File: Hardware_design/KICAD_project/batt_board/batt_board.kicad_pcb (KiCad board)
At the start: 2 copper layers, 50.8 x 50.8 mm, 41 parts, among them J11 battery_plug_in, J2 Conn_01x02, J3 Conn_01x02, J4 Conn_01x02, J5 Conn_01x02, U1 TPS5430DDA, U2 AMS1117-3.3

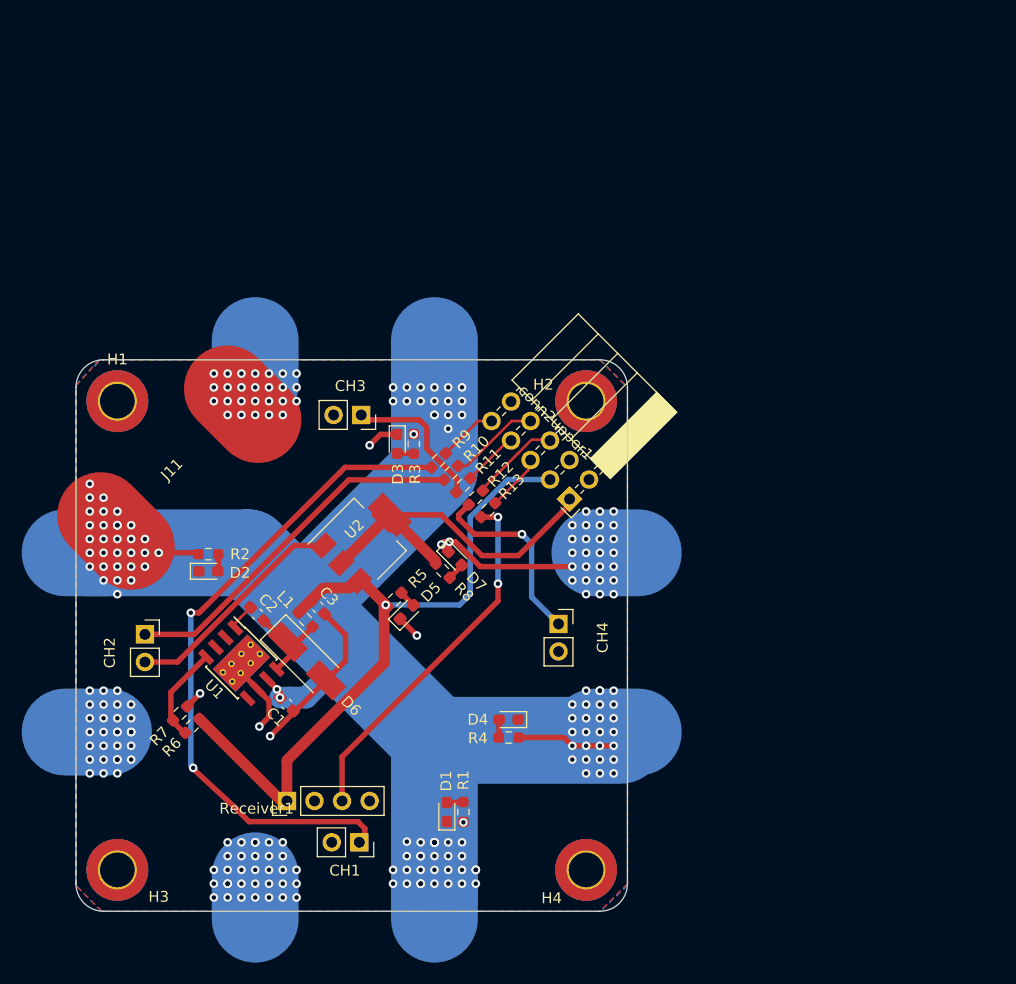
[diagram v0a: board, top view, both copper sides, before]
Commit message: battBoard 打板 control board 设备外设放置
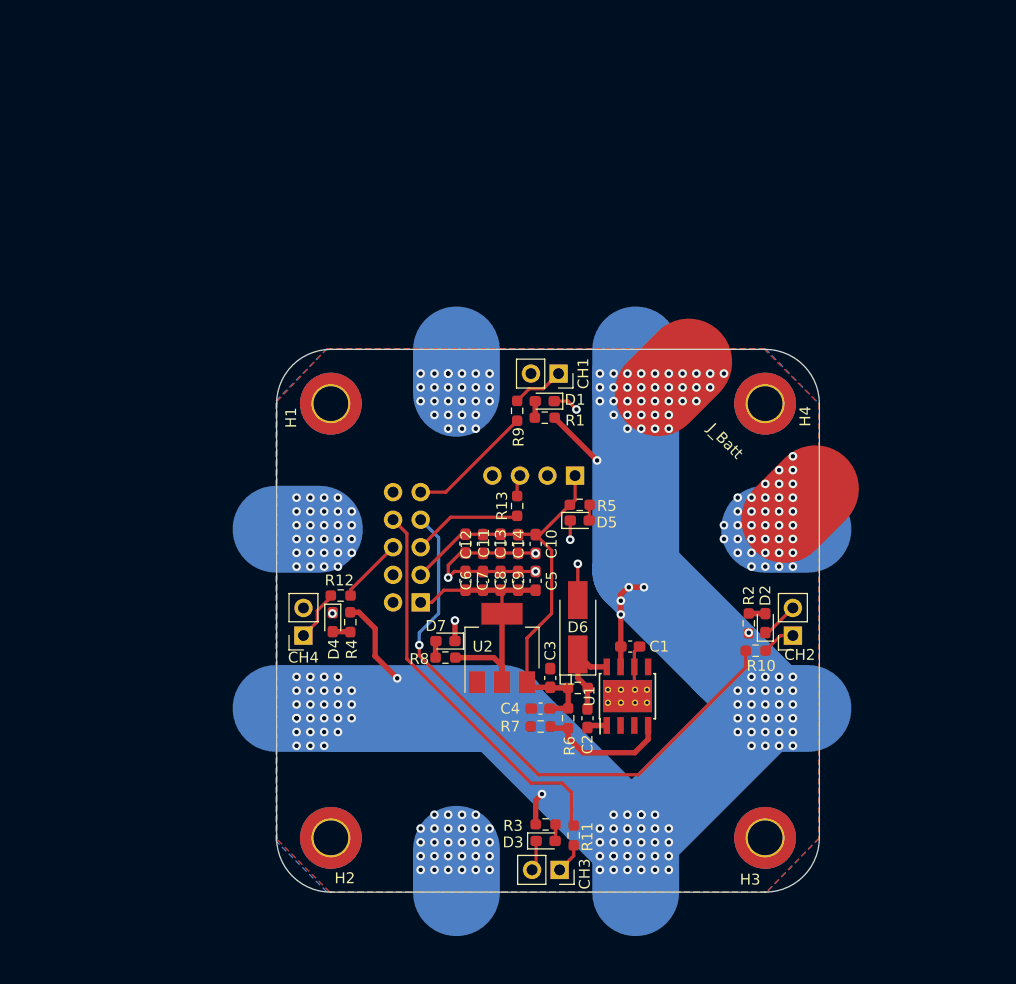
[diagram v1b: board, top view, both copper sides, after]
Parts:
- removed J11: battery_plug_in, Button_Switch_SMD:ESC_Battery_Pale
- added C10: 10uF, Capacitor_SMD:C_0603_1608Metric_Pad1.08x0.95mm_HandSolder, F.Cu at (138.9, 77.9)
- added C11: 100uF, Capacitor_SMD:C_0603_1608Metric_Pad1.08x0.95mm_HandSolder, F.Cu at (134.0, 77.9)
- added C12: 100uF, Capacitor_SMD:C_0603_1608Metric_Pad1.08x0.95mm_HandSolder, F.Cu at (132.4, 77.9)
- added C13: 100uF, Capacitor_SMD:C_0603_1608Metric_Pad1.08x0.95mm_HandSolder, F.Cu at (135.6, 77.9)
- added C14: 100uF, Capacitor_SMD:C_0603_1608Metric_Pad1.08x0.95mm_HandSolder, F.Cu at (137.2, 77.9)
- added C4: 22uF, Capacitor_SMD:C_0603_1608Metric_Pad1.08x0.95mm_HandSolder, F.Cu at (139.3, 93.1)
- added C5: 10uF, Capacitor_SMD:C_0603_1608Metric_Pad1.08x0.95mm_HandSolder, F.Cu at (138.9, 81.3)
- added C6: 100uF, Capacitor_SMD:C_0603_1608Metric_Pad1.08x0.95mm_HandSolder, F.Cu at (132.4, 81.3)
- added C7: 100uF, Capacitor_SMD:C_0603_1608Metric_Pad1.08x0.95mm_HandSolder, F.Cu at (134.0, 81.3)
- added C8: 100uF, Capacitor_SMD:C_0603_1608Metric_Pad1.08x0.95mm_HandSolder, F.Cu at (135.6, 81.3)
- added C9: 100uF, Capacitor_SMD:C_0603_1608Metric_Pad1.08x0.95mm_HandSolder, F.Cu at (137.2, 81.3)
- added J_Batt: battery_plug_in, Button_Switch_SMD:ESC_Battery_Pale, F.Cu at (157.5, 68.6)
- Receiver1, conn2upper1: moved to B.Cu
- moved H3 59.7 mm to (160.0, 105.0)
- moved CH2 59.7 mm to (162.6, 86.4), turned to 180 degrees
- moved J3 52.1 mm to (140.0, 62.0), turned to 0 degrees
- moved D2 51.5 mm to (160.0, 85.2), turned to 90 degrees
- moved R2 50.2 mm to (158.5, 85.2), turned to 270 degrees
- moved CH1 46.9 mm to (141.0, 62.2)
- moved H2 46.6 mm to (120.0, 105.0)
- moved H4 46.0 mm to (160.0, 65.0)
- moved CH3 45.7 mm to (141.1, 108.0)
- moved Receiver1 40.0 mm to (142.5, 71.6)
- moved D3 39.0 mm to (139.8, 105.3), turned to 0 degrees
- moved D1 38.9 mm to (139.7, 64.8), turned to 180 degrees
- moved R3 37.1 mm to (139.8, 103.8), turned to 180 degrees
- moved R1 37.1 mm to (139.7, 66.3), turned to 0 degrees
- moved J2 36.8 mm to (140.0, 108.0)
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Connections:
- conn2upper1 pad 7: Net-(R11-Pad2) -> Net-(R10-Pad2)
- conn2upper1 pad 8: Net-(R10-Pad2) -> Net-(R11-Pad2)
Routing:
- net PWM_CH1: track 61.1 -> 4.85 mm, vias 2 -> 0
- net Net-(R10-Pad2): track 8.39 -> 54.2 mm, vias 0 -> 1
- net Net-(R11-Pad2): track 5.18 -> 36.8 mm
- net PMM: track 33.6 -> 2.17 mm, vias 2 -> 0
- net PWM_CH2: track 33.5 -> 3.10 mm
- net GND: track 65.2 -> 38.7 mm, vias 121 -> 127
- net +5V: track 67.3 -> 42.6 mm, vias 1 -> 0
- net /VCC_IN: track 140.8 -> 119.3 mm, vias 113 -> 129
- net PWM_CH4: track 17.8 -> 4.86 mm, vias 1 -> 0
- net PWM_CH3: track 14.1 -> 2.93 mm
- net +3V3: track 35.9 -> 25.7 mm
- net Net-(R9-Pad2): track 5.47 -> 11.6 mm
- net Net-(R13-Pad1): track 5.00 -> 10.1 mm
- net Net-(R6-Pad2): track 8.75 -> 12.3 mm
- net Net-(R12-Pad2): track 8.40 -> 6.07 mm
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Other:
- board size 50.8 x 50.8 mm -> 50 x 50 mm

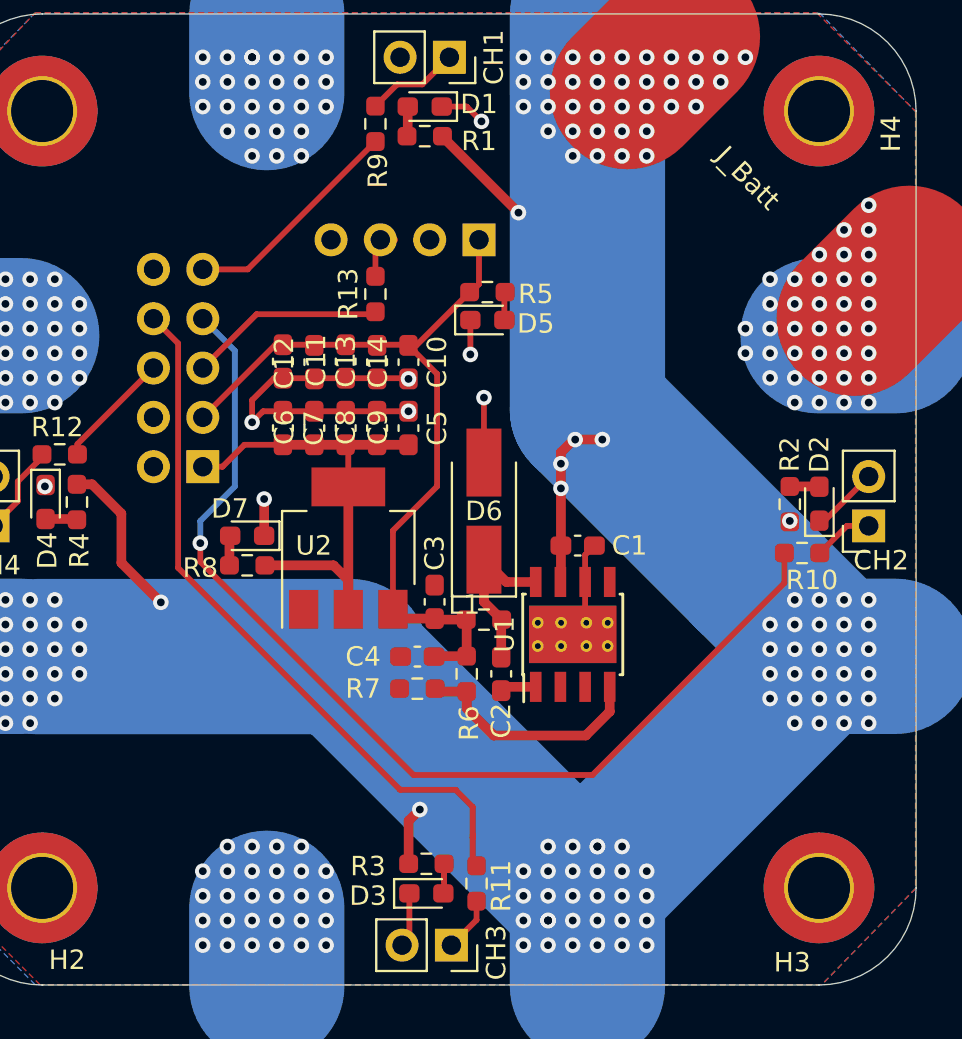
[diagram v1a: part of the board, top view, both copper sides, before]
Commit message: batt board: refine the name of sockets
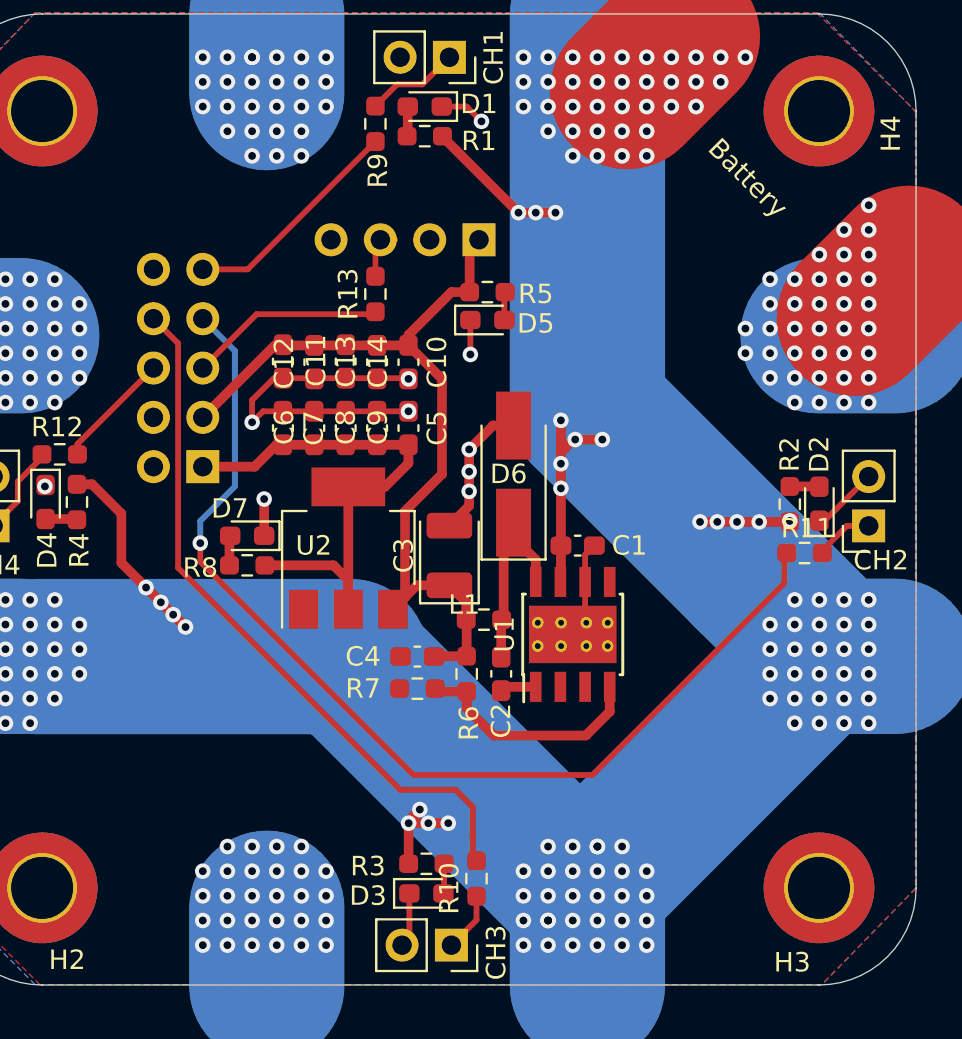
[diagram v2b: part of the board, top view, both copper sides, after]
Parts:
- C11, C12, C13, C14, C6, C7, C8, C9: value 100uF -> 100nF
- C3: footprint Capacitor_SMD:C_0603_1608Metric_Pad1.08x0.95mm_HandSolder -> Capacitor_Tantalum_SMD:CP_EIA-3528-21_Kemet-B
- moved R11 24.0 mm to (159.3, 87.8), turned to 180 degrees
- moved R10 23.7 mm to (142.4, 104.5), turned to 90 degrees
- moved C3 2.51 mm to (141.0, 87.9)
- moved D6 2.44 mm to (144.3, 83.7)
- renumbered J_Batt to Battery, J3 to ESC1, J4 to ESC2, J2 to ESC3, J5 to ESC4
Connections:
- R10 pad 1: PWM_CH2 -> PWM_CH3
- R11 pad 1: PWM_CH3 -> PWM_CH2
- R13 pad 2: PMM -> PPM
- conn2upper1 pad 7: Net-(R10-Pad2) -> Net-(R11-Pad2)
- conn2upper1 pad 8: Net-(R11-Pad2) -> Net-(R10-Pad2)
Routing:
- net Net-(R11-Pad2): track 36.8 -> 54.2 mm, vias 0 -> 1
- net Net-(R10-Pad2): track 54.2 -> 36.8 mm, vias 1 -> 0
- net /VCC_IN: track 119.3 -> 131.9 mm, vias 129 -> 142
- net GND: track 38.7 -> 43.0 mm, vias 127 -> 129
- net +5V: track 42.6 -> 46.2 mm
- net +3V3: track 25.7 -> 28.2 mm
- net Net-(C2-Pad2): track 8.55 -> 10.2 mm
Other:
- board text added: "CH1 CH2 PPM 5V 3.3V"
- board text added: "GND CH3 CH4 NC NC"

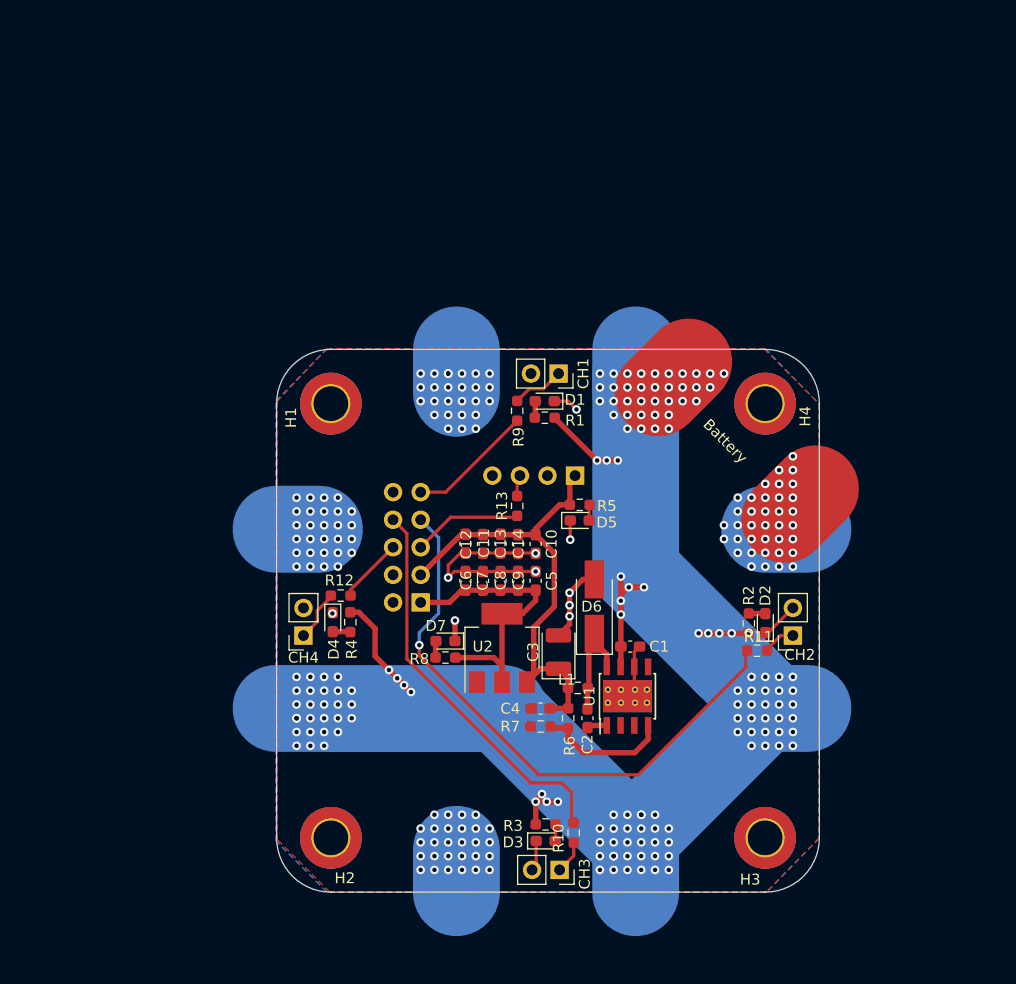
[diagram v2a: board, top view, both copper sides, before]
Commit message: 完善了供电板，增加了 IMU的外围传感电路设计
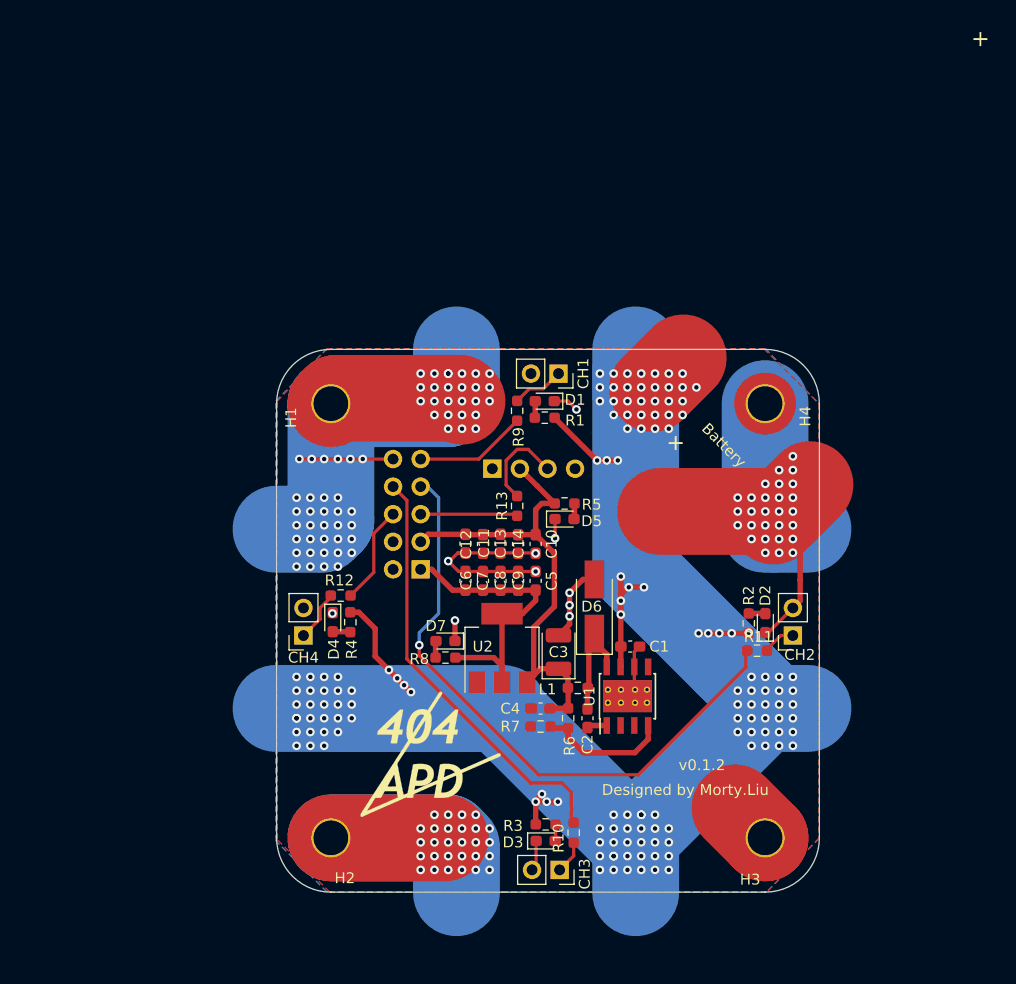
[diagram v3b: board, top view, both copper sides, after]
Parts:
- added G***: LOGO, batt_board:small_404APD, F.Cu at (129.0, 97.4)
- moved Receiver1 7.65 mm to (134.9, 71.0), turned to 270 degrees
- moved conn2upper1 3.05 mm to (128.3, 80.3)
- moved D5 1.40 mm to (141.5, 75.6)
- moved R5 1.40 mm to (141.5, 74.2)
- moved Battery 0.63 mm to (157.0, 68.2)
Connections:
- Receiver1 pad 1: +5V -> GND
- Receiver1 pad 2: GND -> +5V
- Receiver1 pad 3: PMM -> PPM
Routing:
- net GND: track 43.0 -> 171.6 mm, vias 129 -> 126
- net PPM: track 0.00 -> 8.94 mm
- net Net-(R11-Pad2): track 54.2 -> 57.6 mm
- net Net-(R12-Pad2): track 6.07 -> 9.11 mm
- net Net-(R10-Pad2): track 36.8 -> 39.9 mm
- net PMM: track 2.17 -> 0.00 mm
- net Net-(R9-Pad2): track 11.6 -> 10.4 mm
- net +5V: track 46.2 -> 47.4 mm
- net Net-(R13-Pad1): track 10.1 -> 9.13 mm
- net /VCC_IN: vias 142 -> 138
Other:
- net class batt_board added: clearance 0.2, trace_width 0.8, via_dia 0.8, via_drill 0.4
- board text added: "+"
- board text added: "Designed by Morty.Liu"
- board text added: "v0.1.2"
